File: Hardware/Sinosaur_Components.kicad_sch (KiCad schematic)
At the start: 82 parts, among them J1 Conn_01x12_Male, J2 Conn_01x12_Male, J3 Conn_01x16_Male, J4 Conn_01x16_Male, J5 SWD_Header, J6 Eurorack_16_pin_power, J7 UART_Test_Pins, J8 USB_B_Micro, Q1 MMBT3904, Q2 MMBT3904, U1 STM32G473V, U2 STF202-22T1G, U3 TL074, U4 TL074, U5 LT1117-3.3, Y1 8MHz 20pF

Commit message: Updated file names
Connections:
- net +3.3V: now also J3.14 (Pin_14); no longer J2.3 (Pin_3)
- net +3.3VA: now also J2.9 (Pin_9); no longer J2.8 (Pin_8)
- net Clock_In: now also J4.16 (Pin_16); no longer J4.15 (Pin_15)
- net GND: now also J1.10 (Pin_10), J2.10 (Pin_10), J2.3 (Pin_3), J3.13 (Pin_13), J3.15 (Pin_15), J3.6 (Pin_6), J4.8 (Pin_8); no longer J2.9 (Pin_9), J4.16 (Pin_16)
- net Gate_In: now also J4.15 (Pin_15); no longer J4.14 (Pin_14)
- net Sine1_Inv_Out: now also J2.8 (Pin_8); no longer J2.7 (Pin_7)
- net Sine1_Lvl_Btn: now also J4.14 (Pin_14); no longer J4.13 (Pin_13)
- net Sine1_Out: now also J2.7 (Pin_7); no longer J2.6 (Pin_6)
- net Sine1_Ramp_Lvl_LED: now also J3.4 (Pin_4); no longer J3.3 (Pin_3)
- net Sine1_Rate: now also J2.11 (Pin_11); no longer J2.10 (Pin_10)
- net Sine1_Rate_Btn: now also J4.11 (Pin_11); no longer J4.10 (Pin_10)
- net Sine1_Swell_Lvl_LED: now also J3.8 (Pin_8); no longer J3.6 (Pin_6)
- net Sine1_Swell_Rate_LED: now also J3.1 (Pin_1); no longer J1.12 (Pin_12)
- net Sine2_Lvl_Btn: now also J4.13 (Pin_13); no longer J4.12 (Pin_12)
- net Sine2_Ramp_Lvl_LED: now also J3.5 (Pin_5); no longer J3.4 (Pin_4)
- net Sine2_Ramp_Rate_LED: now also J4.6 (Pin_6); no longer J3.9 (Pin_9)
- net Sine2_Rate: now also J3.12 (Pin_12)
- net Sine2_Rate_Btn: now also J4.10 (Pin_10); no longer J4.9 (Pin_9)
- net Sine2_Swell_Lvl_LED: now also J3.9 (Pin_9); no longer J3.8 (Pin_8)
- net Sine2_Swell_Rate_LED: now also J1.12 (Pin_12); no longer J3.7 (Pin_7)
- net Sine3_LED: now also J4.7 (Pin_7); no longer J4.6 (Pin_6)
- net Sine3_Level: now also J2.6 (Pin_6); no longer J2.11 (Pin_11)
- net Sine3_Lvl_Btn: now also J4.12 (Pin_12); no longer J4.11 (Pin_11)
- net Sine3_Ramp_Lvl_LED: now also J3.7 (Pin_7); no longer J3.5 (Pin_5)
- net Sine3_Ramp_Rate_LED: now also J3.3 (Pin_3); no longer J3.2 (Pin_2)
- net Sine3_Rate_Btn: now also J4.9 (Pin_9); no longer J4.8 (Pin_8)
- net Swell_Rate: now also J3.2 (Pin_2); no longer J3.1 (Pin_1)

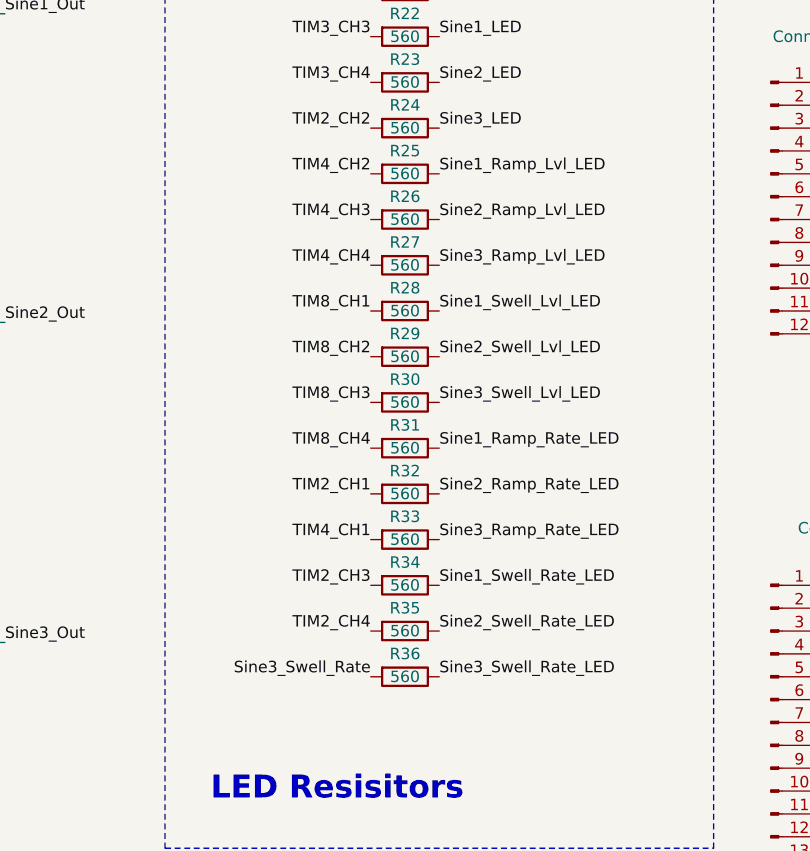
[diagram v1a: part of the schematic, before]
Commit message: Started control layout
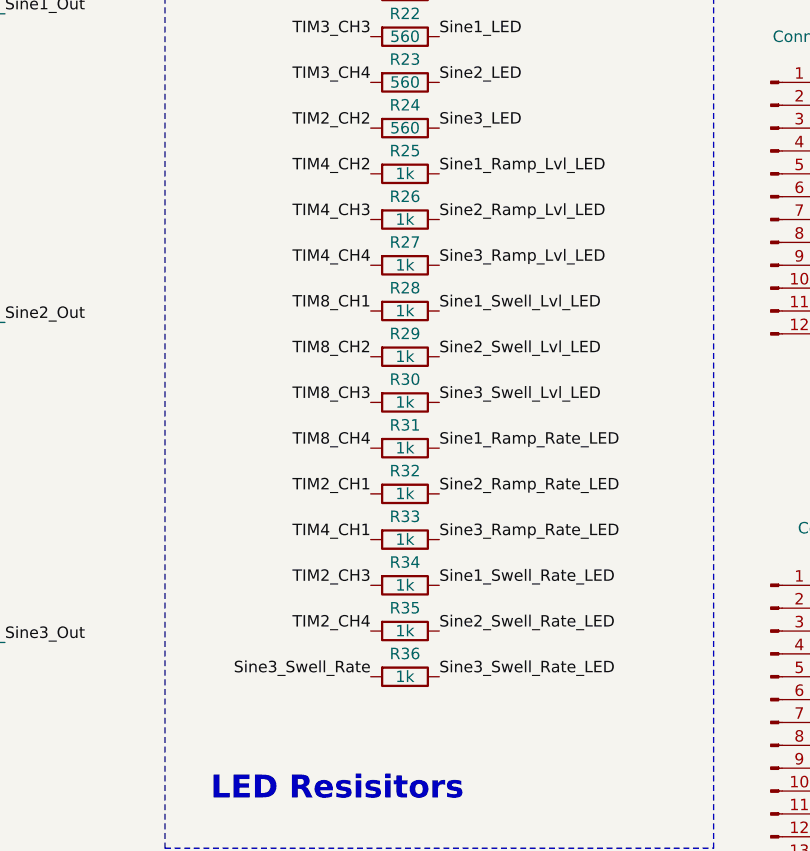
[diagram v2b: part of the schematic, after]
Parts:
- R25, R26, R27, R28, R29, R30, R31, R32, R33, R34, R35, R36: value 560 -> 1k
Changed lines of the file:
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@@
 			)
 		)
-		(property "Value" "560"
+		(property "Value" "1k "
 			(at 260.35 88.9 90)
 			(effects
@@
 			)
 		)
-		(property "Value" "560"
+		(property "Value" "1k "
 			(at 260.35 73.66 90)
 			(effects
@@
 			)
 		)
-		(property "Value" "560"
+		(property "Value" "1k "
 			(at 260.35 63.5 90)
 			(effects
@@
 			)
 		)
-		(property "Value" "560"
+		(property "Value" "1k "
 			(at 260.35 68.58 90)
 			(effects
@@
 			)
 		)
-		(property "Value" "560"
+		(property "Value" "1k "
 			(at 260.35 53.34 90)
 			(effects
@@
 			)
 		)
-		(property "Value" "560"
+		(property "Value" "1k "
 			(at 260.35 93.98 90)
 			(effects
@@
 			)
 		)
-		(property "Value" "560"
+		(property "Value" "1k "
 			(at 260.35 58.42 90)
 			(effects
@@
 			)
 		)
-		(property "Value" "560"
+		(property "Value" "1k "
 			(at 260.35 78.74 90)
 			(effects
@@
 			)
 		)
-		(property "Value" "560"
+		(property "Value" "1k "
 			(at 260.35 104.14 90)
 			(effects
@@
 			)
 		)
-		(property "Value" "560"
+		(property "Value" "1k "
 			(at 260.35 99.06 90)
 			(effects
@@
 			)
 		)
-		(property "Value" "560"
+		(property "Value" "1k "
 			(at 260.35 83.82 90)
 			(effects
@@
 			)
 		)
-		(property "Value" "560"
+		(property "Value" "1k"
 			(at 260.35 48.26 90)
 			(effects

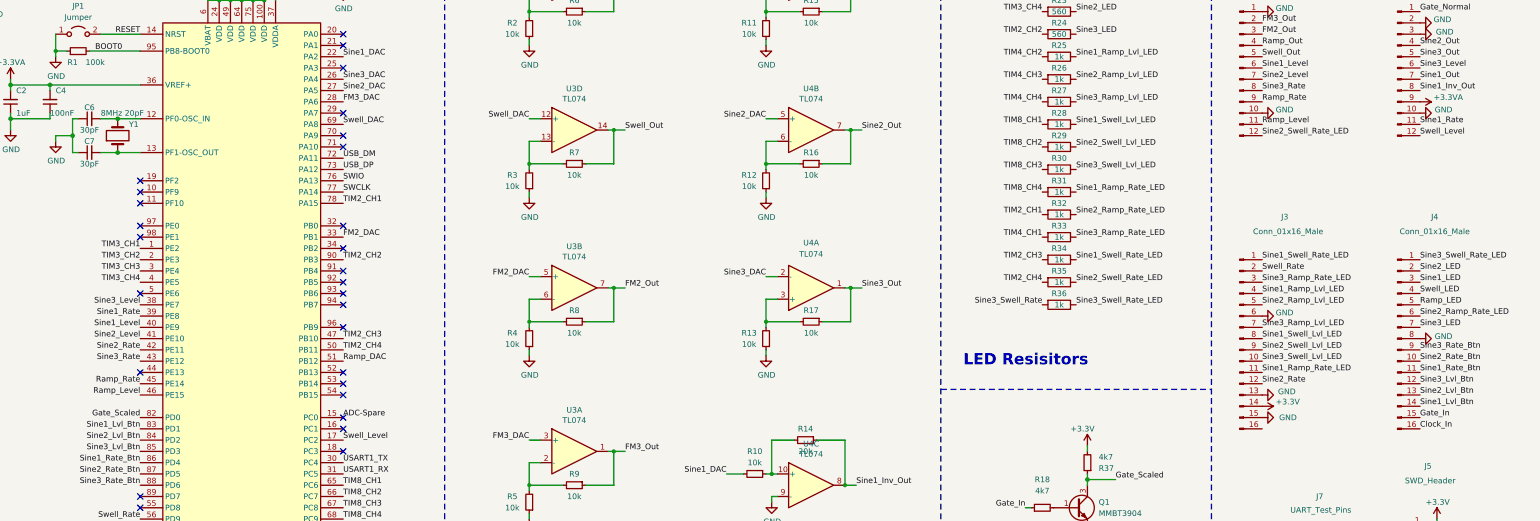
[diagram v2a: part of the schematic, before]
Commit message: Control PCB wiring
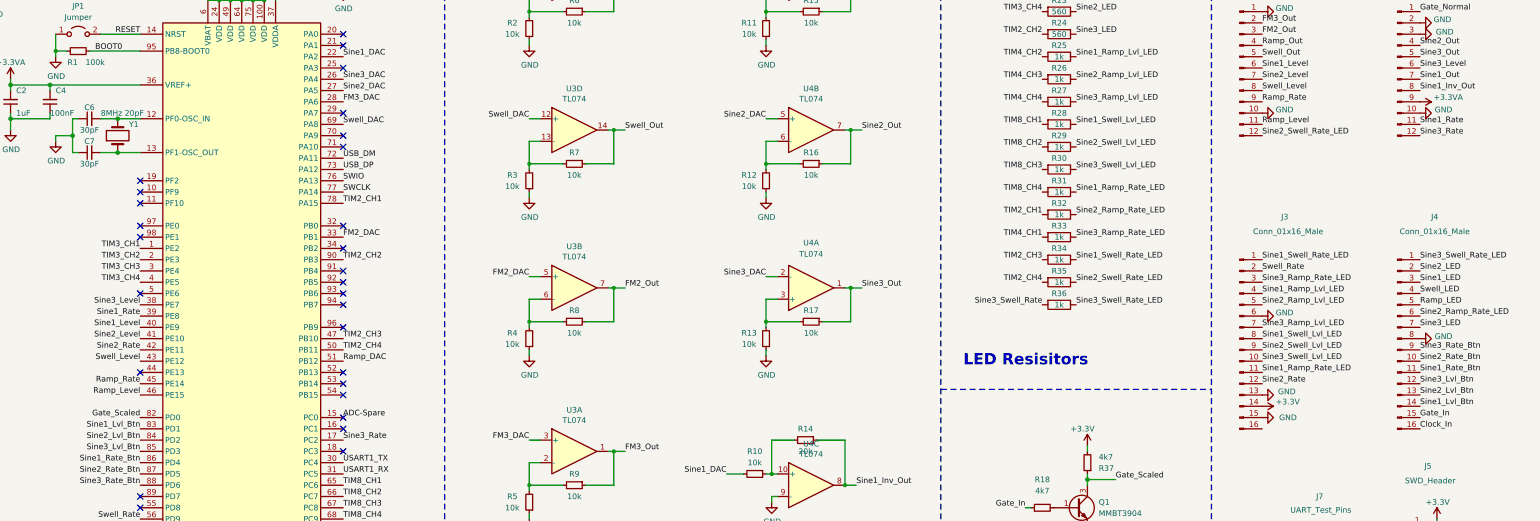
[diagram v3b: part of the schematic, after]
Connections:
- net Sine3_Rate: now also J2.12 (Pin_12), U1.17 (PC2); no longer J1.8 (Pin_8), U1.43 (PE12)
- net Swell_Level: now also J1.8 (Pin_8), U1.43 (PE12); no longer J2.12 (Pin_12), U1.17 (PC2)
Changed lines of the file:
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@@
 	)
 	(label "Swell_Level"
-		(at 341.63 66.04 0)
+		(at 306.07 55.88 0)
 		(fields_autoplaced yes)
 		(effects
@@
 	)
 	(label "Swell_Level"
-		(at 99.06 134.62 0)
-		(fields_autoplaced yes)
-		(effects
-			(font
-				(size 1.27 1.27)
-			)
-			(justify left bottom)
+		(at 53.34 116.84 180)
+		(fields_autoplaced yes)
+		(effects
+			(font
+				(size 1.27 1.27)
+			)
+			(justify right bottom)
 		)
 	)
@@
 	)
 	(label "Sine3_Rate"
-		(at 53.34 116.84 180)
-		(fields_autoplaced yes)
-		(effects
-			(font
-				(size 1.27 1.27)
-			)
-			(justify right bottom)
+		(at 99.06 134.62 0)
+		(fields_autoplaced yes)
+		(effects
+			(font
+				(size 1.27 1.27)
+			)
+			(justify left bottom)
 		)
 	)
@@
 	)
 	(label "Sine3_Rate"
-		(at 306.07 55.88 0)
-		(fields_autoplaced yes)
-		(effects
+		(at 341.63 66.04 0)
+		(fields_autoplaced yes)
+		(effects

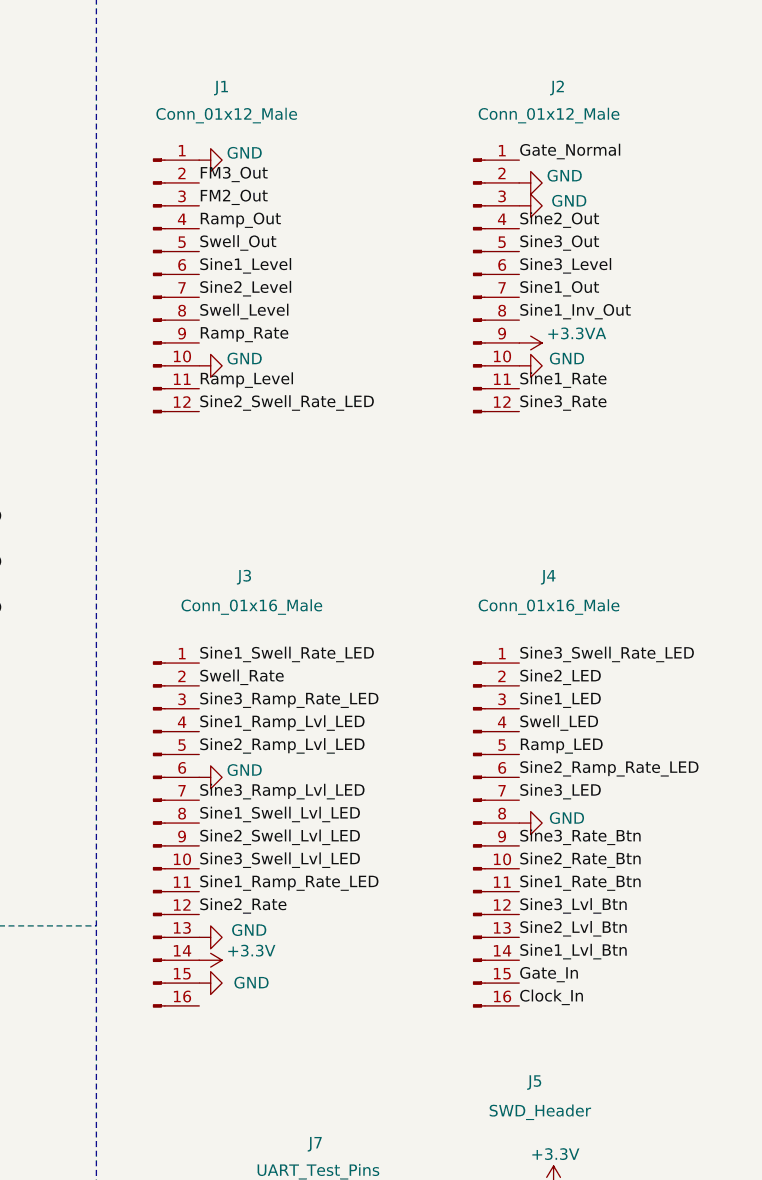
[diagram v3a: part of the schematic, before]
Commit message: Updates to LEDs
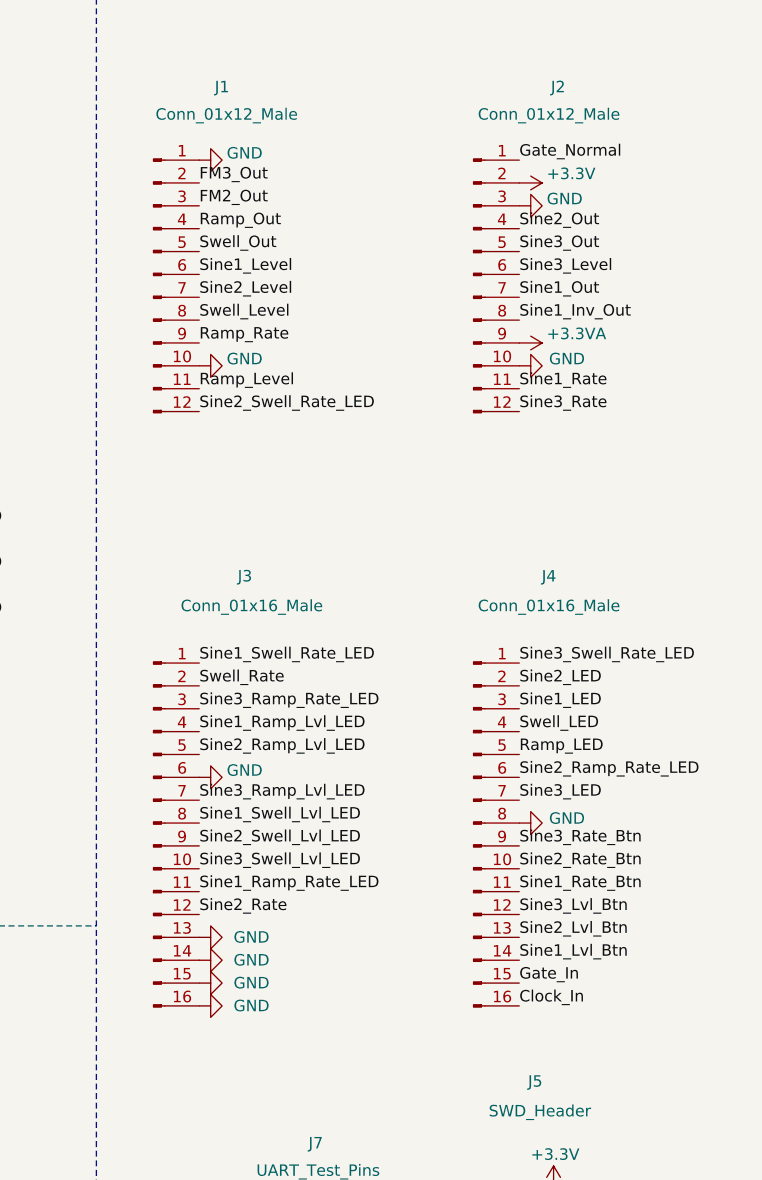
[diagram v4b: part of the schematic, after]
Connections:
- net +3.3V: now also J2.2 (Pin_2); no longer J3.14 (Pin_14)
- net GND: now also J3.14 (Pin_14), J3.16 (Pin_16); no longer J2.2 (Pin_2)
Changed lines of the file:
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@@
 	)
 	(symbol
+		(lib_id "power:+3.3V")
+		(at 341.63 40.64 270)
+		(unit 1)
+		(exclude_from_sim no)
+		(in_bom yes)
+		(on_board yes)
+		(dnp no)
+		(property "Reference" "#PWR04"
+			(at 337.82 40.64 0)
+			(effects
+				(font
+					(size 1.27 1.27)
+				)
+				(hide yes)
+			)
+		)
+		(property "Value" "+3.3V"
+			(at 344.678 39.624 90)
+			(effects
+				(font
+					(size 1.27 1.27)
+				)
+				(justify left)
+			)
+		)
+		(property "Footprint" ""
+			(at 341.63 40.64 0)
+			(effects
+				(font
+					(size 1.27 1.27)
+				)
+				(hide yes)
+			)
+		)
+		(property "Datasheet" ""
+			(at 341.63 40.64 0)
+			(effects
+				(font
+					(size 1.27 1.27)
+				)
+				(hide yes)
+			)
+		)
+		(property "Description" "Power symbol creates a global label with name \"+3.3V\""
+			(at 341.63 40.64 0)
+			(effects
+				(font
+					(size 1.27 1.27)
+				)
+				(hide yes)
+			)
+		)
+		(pin "1"
+		)
+		(instances
+			(project "Sinosaur_Components"
+				(path "/ea88d275-24e2-4917-9451-7e51068364d9"
+					(reference "#PWR04")
+					(unit 1)
+				)
+			)
+		)
+	)
+	(symbol
 		(lib_id "Device:R_Small")
 		(at 204.47 38.1 270)
@@
 	)
 	(symbol
+		(lib_id "power:GND")
+		(at 306.07 132.08 90)
+		(unit 1)
+		(exclude_from_sim no)
+		(in_bom yes)
+		(on_board yes)
+		(dnp no)
+		(fields_autoplaced yes)
+		(property "Reference" "#PWR030"
+			(at 312.42 132.08 0)
+			(effects
+				(font
+					(size 1.27 1.27)
+				)
+				(hide yes)
+			)
+		)
+		(property "Value" "GND"
+			(at 309.88 132.0799 90)
+			(effects
+				(font
+					(size 1.27 1.27)
+				)
+				(justify right)
+			)
+		)
+		(property "Footprint" ""
+			(at 306.07 132.08 0)
+			(effects
+				(font
+					(size 1.27 1.27)
+				)
+				(hide yes)
+			)
+		)
+		(property "Datasheet" ""
+			(at 306.07 132.08 0)
+			(effects
+				(font
+					(size 1.27 1.27)
+				)
+				(hide yes)
+			)
+		)
+		(property "Description" "Power symbol creates a global label with name \"GND\" , ground"
+			(at 306.07 132.08 0)
+			(effects
+				(font
+					(size 1.27 1.27)
+				)
+				(hide yes)
+			)
+		)
+		(pin "1"
+		)
+		(instances
+			(project "Sinosaur_Components"
+				(path "/ea88d275-24e2-4917-9451-7e51068364d9"
+					(reference "#PWR030")
+					(unit 1)
+				)
+			)
+		)
+	)
+	(symbol
 		(lib_id "Device:R_Small")
 		(at 194.31 41.91 180)
@@
 		(on_board yes)
 		(dnp no)
+		(fields_autoplaced yes)
 		(property "Reference" "#PWR03"
 			(at 312.42 124.46 0)
@@
 		)
 		(property "Value" "GND"
-			(at 309.626 123.698 90)
+			(at 309.88 124.4599 90)
 			(effects
 				(font
@@
 	)
 	(symbol
-		(lib_id "power:GND")
-		(at 341.63 43.18 90)
+		(lib_id "power:+3.3VA")
+		(at 24.13 53.34 0)
 		(unit 1)
 		(exclude_from_sim no)
@@
 		(on_board yes)
 		(dnp no)
-		(property "Reference" "#PWR030"
-			(at 347.98 43.18 0)
+		(fields_autoplaced yes)
+		(property "Reference" "#PWR017"
+			(at 24.13 57.15 0)
 			(effects
 				(font
@@
 			)
 		)
-		(property "Value" "GND"
-			(at 345.186 42.672 90)
+		(property "Value" "+3.3VA"
+			(at 24.13 49.53 0)
 			(effects
 				(font
 					(size 1.27 1.27)
 				)
-				(justify right)
 			)
 		)
 		(property "Footprint" ""
-			(at 341.63 43.18 0)
+			(at 24.13 53.34 0)
 			(effects
 				(font
@@
 		)
 		(property "Datasheet" ""
-			(at 341.63 43.18 0)
+			(at 24.13 53.34 0)
 			(effects
 				(font
@@
 			)
 		)
-		(property "Description" "Power symbol creates a global label with name \"GND\" , ground"
-			(at 341.63 43.18 0)
+		(property "Description" "Power symbol creates a global label with name \"+3.3VA\""
+			(at 24.13 53.34 0)
 			(effects
 				(font
@@
 		)
 		(instances
-			(project "Uncertain_Times_Components"
+			(project "Quango_Components"
 				(path "/ea88d275-24e2-4917-9451-7e51068364d9"
-					(reference "#PWR030")
+					(reference "#PWR017")
 					(unit 1)
 				)
@@
 	)
 	(symbol
-		(lib_id "power:+3.3VA")
-		(at 24.13 53.34 0)
+		(lib_id "power:GND")
+		(at 306.07 127 90)
 		(unit 1)
 		(exclude_from_sim no)
@@
 		(dnp no)
 		(fields_autoplaced yes)
-		(property "Reference" "#PWR017"
-			(at 24.13 57.15 0)
+		(property "Reference" "#PWR05"
+			(at 312.42 127 0)
 			(effects
 				(font
@@
 			)
 		)
-		(property "Value" "+3.3VA"
-			(at 24.13 49.53 0)
+		(property "Value" "GND"
+			(at 309.88 126.9999 90)
 			(effects
 				(font
 					(size 1.27 1.27)
 				)
+				(justify right)
 			)
 		)
 		(property "Footprint" ""
-			(at 24.13 53.34 0)
+			(at 306.07 127 0)
 			(effects
 				(font
@@
 		)
 		(property "Datasheet" ""
-			(at 24.13 53.34 0)
+			(at 306.07 127 0)
 			(effects
 				(font
@@
 			)
 		)
-		(property "Description" "Power symbol creates a global label with name \"+3.3VA\""
-			(at 24.13 53.34 0)
+		(property "Description" "Power symbol creates a global label with name \"GND\" , ground"
+			(at 306.07 127 0)
 			(effects
 				(font
@@
 		)
 		(instances
-			(project "Quango_Components"
+			(project "Sinosaur_Components"
 				(path "/ea88d275-24e2-4917-9451-7e51068364d9"
-					(reference "#PWR017")
+					(reference "#PWR05")
 					(unit 1)
 				)
@@
 	(symbol
 		(lib_id "power:GND")
-		(at 341.63 40.64 90)
+		(at 341.63 43.18 90)
 		(unit 1)
 		(exclude_from_sim no)
@@
 		(dnp no)
 		(property "Reference" "#PWR09"
-			(at 347.98 40.64 0)
+			(at 347.98 43.18 0)
 			(effects
 				(font
@@
 		)
 		(property "Value" "GND"
-			(at 344.678 39.878 90)
+			(at 344.678 42.418 90)
 			(effects
 				(font
@@
 		)
 		(property "Footprint" ""
-			(at 341.63 40.64 0)
+			(at 341.63 43.18 0)
 			(effects
 				(font
@@
 		)
 		(property "Datasheet" ""
-			(at 341.63 40.64 0)
+			(at 341.63 43.18 0)
 			(effects
 				(font
@@
 		)
 		(property "Description" "Power symbol creates a global label with name \"GND\" , ground"
-			(at 341.63 40.64 0)
+			(at 341.63 43.18 0)
 			(effects
 				(font
@@
 					(unit 1)
 				)
-			)
-		)
-	)
-	(symbol
-		(lib_id "power:+3.3V")
-		(at 306.07 127 270)
-		(unit 1)
-		(exclude_from_sim no)
-		(in_bom yes)
-		(on_board yes)
-		(dnp no)
-		(property "Reference" "#PWR054"
-			(at 302.26 127 0)
-			(effects
-				(font
-					(size 1.27 1.27)
-				)
-				(hide yes)
-			)
-		)
-		(property "Value" "+3.3V"
-			(at 309.118 125.984 90)
-			(effects
-				(font
-					(size 1.27 1.27)
-				)
-				(justify left)
-			)
-		)
-		(property "Footprint" ""
-			(at 306.07 127 0)
-			(effects
-				(font
-					(size 1.27 1.27)
-				)
-				(hide yes)
-			)
-		)
-		(property "Datasheet" ""
-			(at 306.07 127 0)
-			(effects
-				(font
-					(size 1.27 1.27)
-				)
-				(hide yes)
-			)
-		)
-		(property "Description" "Power symbol creates a global label with name \"+3.3V\""
-			(at 306.07 127 0)
-			(effects
-				(font
-					(size 1.27 1.27)
-				)
-				(hide yes)
-			)
-		)
-		(pin "1"
-		)
-		(instances
-			(project "Uncertain_Times_Components"
-				(path "/ea88d275-24e2-4917-9451-7e51068364d9"
-					(reference "#PWR054")
-					(unit 1)
-				)
